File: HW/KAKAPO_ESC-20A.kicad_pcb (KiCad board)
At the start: 4 copper layers, 86.5 x 28 mm, 88 parts, among them M1 Mount_M3, M2 Mount_M3, M3 Mount_M3, M4 Mount_M3, U1 DRV8244S-Q1, U2 DRV8244S-Q1, U3 LR7533-T, U4 SK1117-ADJ, U5 STM32C011F4P6

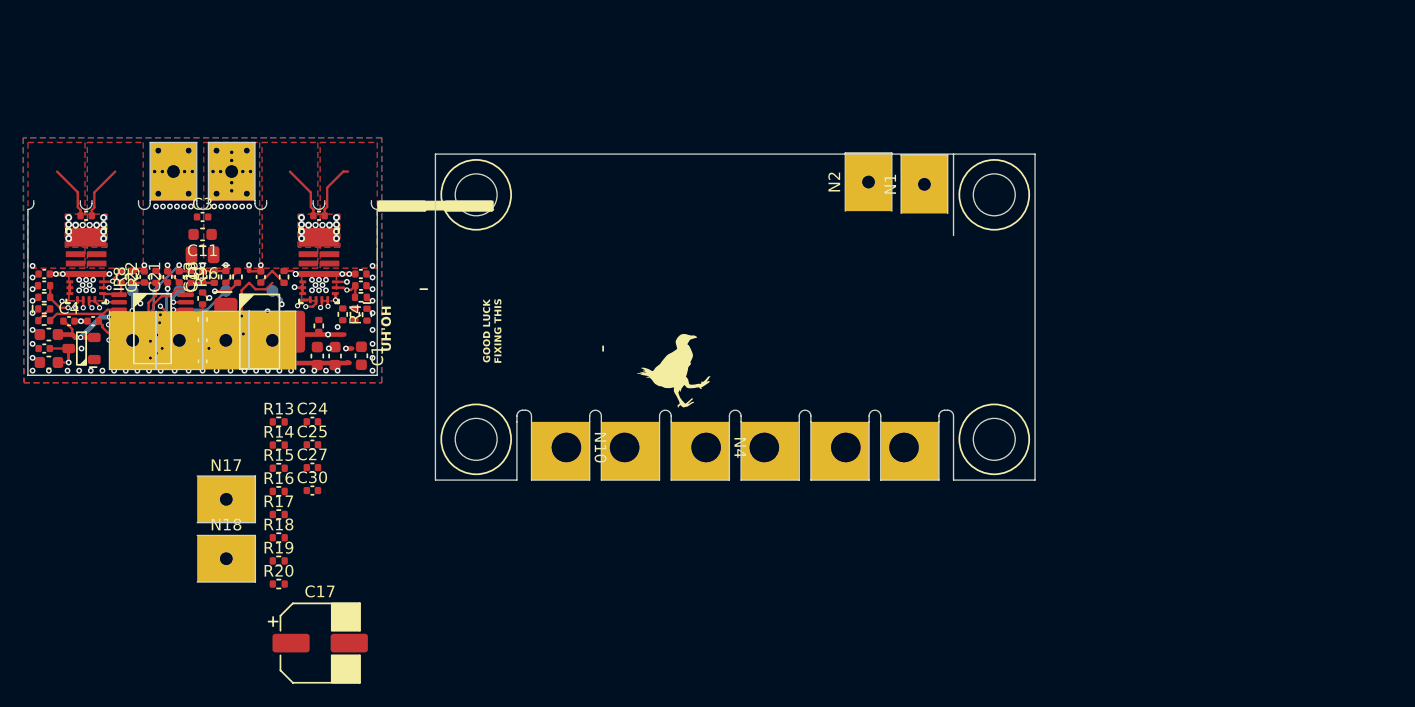
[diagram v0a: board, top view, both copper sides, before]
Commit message: WIP - Layout Motor Drivers + Buck Circuit
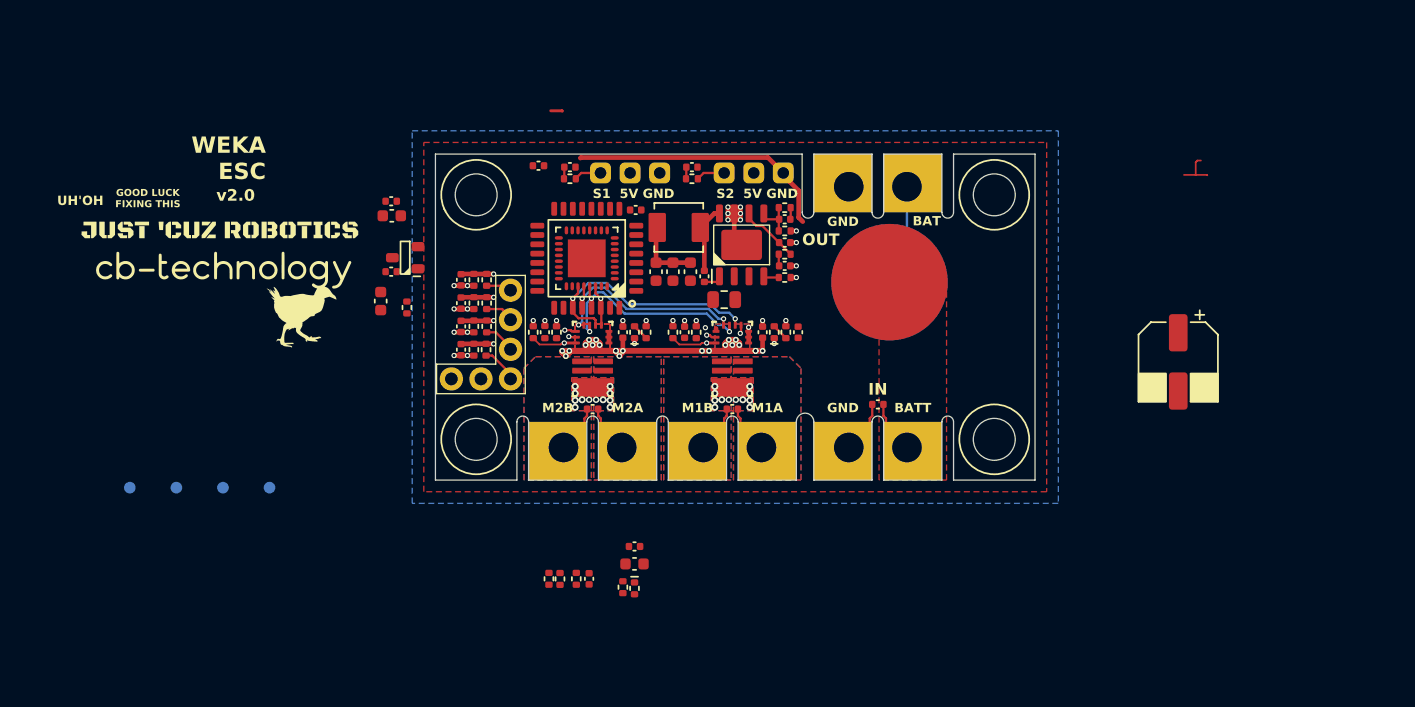
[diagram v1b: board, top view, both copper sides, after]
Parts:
- removed C10, C21: 100nF 50V, C_Capacitor:C_0402
- removed C12, C15: 22uF 10V, C_Capacitor:C_0603
- removed the G*** at (221.2, 118.8)
- removed N11, N12, N17, N18, N5, N6, N7, N8: Finger_4x5_M1, N_NonPart:Finger_4x5_M1
- removed R27: 732 1%, R_Resistor:R_0402
- removed U4: SK1117-ADJ, U_IC:SOT223_3
- added A1: Radio_FS2A, A_Assembly:Radio_FS2A, F.Cu at (200.1, 110.0)
- added C26: 100nF 50V, C_Capacitor:C_0402, F.Cu at (238.0, 121.5)
- added C31: 39pF 50V, C_Capacitor:C_0402, F.Cu at (230.0, 105.6)
- added C33: 22uF 10V, C_Capacitor:C_0603, F.Cu at (221.9, 110.1)
- added C34: 22uF 10V, C_Capacitor:C_0603, F.Cu at (220.4, 110.1)
- added C35: 22uF 10V, C_Capacitor:C_0603, F.Cu at (218.9, 110.1)
- added C37: 100nF 50V, C_Capacitor:C_0402, F.Cu at (231.2, 115.3)
- added C38: 100nF 50V, C_Capacitor:C_0402, F.Cu at (217.2, 104.8)
- added J1: Pins_2.54_1x3, J_Connector:Pins-2.54-1x3, F.Cu at (214.2, 101.6)
- added J2: Pins_2.54_1x3, J_Connector:Pins-2.54-1x3, F.Cu at (224.8, 101.6)
- added L1: 1.5uH, L_Inductor:L_4.2x4.2, F.Cu at (220.9, 106.3)
- added R21: 115.8K 1%, R_Resistor:R_0402, F.Cu at (230.0, 104.6)
- added R22: 22.1K 1%, R_Resistor:R_0402, F.Cu at (230.0, 106.6)
- added R23: 100K 1%, R_Resistor:R_0402, F.Cu at (230.0, 110.6)
- added S1: Twist_Switch_M4, CombatParts:Twist_Switch_M4, F.Cu at (239.0, 111.0)
- added U6: STM32C031KxTx, U_IC:LQFP32_08_7x7, F.Cu at (213.0, 109.0)
- added U7: STM32C031KxUx, U_IC:QFN32_05_5x5_EP, F.Cu at (213.0, 109.0)
- C1: value 22uF 10V -> 39pF 50V; footprint C_Capacitor:C_0603 -> C_Capacitor:C_0402
- C16: value 10uF 50V -> 22uF 10V; footprint C_Capacitor:C_0805 -> C_Capacitor:C_0603
- C6: value 100nF 50V -> 2.7nF 50V
- C9: value 10uF 35V -> 10uF 50V; footprint C_Capacitor:C_0603 -> C_Capacitor:C_0805
- G*** (x3), N13: moved to F.Cu
- N1, N14: moved to B.Cu
- R2: value 243 1% -> 15.8K 1%
- U5: value STM32C011F4P6 -> AP64500SP-13; footprint U_IC:TSSOP20_4.4mm -> U_IC:SOIC_8_EP
- moved C17 77.6 mm to (263.8, 117.8), turned to -90 degrees
- moved R12 51.7 mm to (218.1, 115.3), turned to -90 degrees
- moved U5 51.1 mm to (226.3, 107.8), turned to 90 degrees
- moved DS1 50.7 mm to (217.1, 115.3), turned to 90 degrees
- moved C6 50.7 mm to (230.0, 109.6), turned to 0 degrees
- moved R2 50.3 mm to (230.0, 108.6), turned to 180 degrees
- moved C20 50.0 mm to (216.1, 115.3), turned to 90 degrees
- moved R18 47.0 mm to (222.0, 102.1), turned to 180 degrees
- moved C11 46.7 mm to (217.1, 135.2)
- moved C3 46.7 mm to (217.1, 133.7)
- moved C8 46.6 mm to (213.5, 121.9), turned to 180 degrees
- moved U2 44.2 mm to (213.5, 117.6), turned to 0 degrees
- moved DS2 44.1 mm to (217.1, 137.3)
- moved R3 44.1 mm to (210.4, 115.3), turned to 90 degrees
- moved C19 43.2 mm to (209.4, 115.3), turned to 90 degrees
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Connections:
- C1 pad 1: +5V -> Net-(U5-COMP)
- C16 pad 1: VCC -> Net-(U3-VIN)
- C2 pad 1: +5V -> Net-(U3-VIN)
- C24 pad 1: VCC -> Net-(U5-BST)
- C24 pad 2: GND -> Net-(U5-SW)
- C6 pad 1: Net-(U4-VIN) -> Net-(C6-Pad1)
- C9 pad 1: Net-(U4-VIN) -> VCC
- D1 pad 1: Net-(U4-VIN) -> Net-(U3-VIN)
- D1 pad 2: VCC -> +5V
- N1 pad 1: +BATT -> Net-(C26-Pad1)
- R2 pad 1: +5V -> Net-(U5-COMP)
- R2 pad 2: Net-(U4-ADJ) -> Net-(C6-Pad1)
- U3 pad 3: +5V -> Net-(U3-VIN)
- U5 pad 1: MOTOR_B_nFAULT -> Net-(U5-BST)
- U5 pad 2: MOTOR_B_nSCS -> VCC
- U5 pad 3: LED_M2 -> VCC
- U5 pad 4: +3V3 -> Net-(U5-RT/CLK)
- U5 pad 5: GND -> Net-(U5-FB)
- U5 pad 6: /MCU/nRST -> Net-(U5-COMP)
- U5 pad 7: MOTOR_B_SNS -> GND
- U5 pad 8: RADIO_CH1 -> Net-(U5-SW)
- U5 pad 9: RADIO_CH2 -> GND
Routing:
- net +3V3: track 46.6 -> 8.24 mm, vias 6 -> 2
- net +5V: track 44.0 -> 7.03 mm, vias 3 -> 0
- net VCC: track 21.0 -> 50.6 mm, vias 31 -> 22
- net MOTOR_A_SNS: track 25.1 -> 0.92 mm, vias 2 -> 1
- net LED_M1: track 19.9 -> 0.49 mm
- net MOTOR_A_nFAULT: track 19.4 -> 0.66 mm
- net GND: track 69.6 -> 52.8 mm, vias 88 -> 51
- net (no net): track 16.5 -> 0.00 mm
- net MOTOR_A_nSCS: track 16.7 -> 0.81 mm, vias 2 -> 1
- net V_BATT: track 15.6 -> 0.00 mm, vias 2 -> 0
- net Net-(U4-VIN): track 14.2 -> 0.00 mm
- net MOTOR_B_SNS: track 14.2 -> 0.68 mm, vias 3 -> 1
- net MOTOR_SCLK: track 32.2 -> 21.4 mm, vias 3 -> 2
- net MOTOR_SDI: track 30.0 -> 19.8 mm
- net RADIO_CH2: track 12.1 -> 2.82 mm, vias 0 -> 1
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- added copper zone on In2.Cu, net GND
- added copper zone on B.Cu, net MOTOR_A+
- added copper zone on B.Cu, net MOTOR_A-
- added copper zone on B.Cu, net MOTOR_B+
- added copper zone on B.Cu, net MOTOR_B-
- added copper zone on F.Cu, net Net-(C26-Pad1)
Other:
- board size 86.5 x 28 mm -> 51.5 x 28 mm
- board text added: "BAT"
- board text added: "IN"
- board text added: "OUT"
- board text removed: "+"
- board text removed: "-"

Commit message: WIP - Continue Tracking MCU
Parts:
- added C10: 100nF 50V, C_Capacitor:C_0402, F.Cu at (238.0, 106.5)
- moved C16 11.8 mm to (206.1, 107.8), turned to 0 degrees
- moved D1 11.2 mm to (206.7, 106.6), turned to 0 degrees
- moved C5 10.6 mm to (206.1, 109.3), turned to 0 degrees
- moved C4 10.4 mm to (203.8, 111.2)
- moved C14 7.86 mm to (214.9, 96.0)
- moved C2 5.71 mm to (201.8, 111.2)
- moved U3 5.40 mm to (202.8, 109.0), turned to 90 degrees
- moved R8 2.45 mm to (203.8, 113.2), turned to 0 degrees
- moved R16 1.62 mm to (201.8, 116.2), turned to 180 degrees
- moved R9 1.55 mm to (201.8, 113.2), turned to 180 degrees
- moved R13 1.52 mm to (203.8, 114.2), turned to 180 degrees
- moved R6 1.52 mm to (203.8, 112.2), turned to 180 degrees
- moved S1 1.50 mm to (239.0, 112.5)
- moved R7 1.49 mm to (203.8, 116.2), turned to 0 degrees
- moved C13 1.46 mm to (201.8, 114.2), turned to 180 degrees
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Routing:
- net Net-(U3-VIN): track 0.00 -> 8.51 mm
- net GND: track 52.8 -> 58.5 mm, vias 51 -> 132
- net VCC: track 50.6 -> 56.2 mm
- net MOTOR_A_nFAULT: track 0.66 -> 4.57 mm
- net /MCU/PA15: track 0.00 -> 3.79 mm, vias 0 -> 1
- net Net-(U5-FB): track 7.35 -> 3.73 mm
- net MOTOR_B_nFAULT: track 1.52 -> 4.57 mm
- net LED_M2: track 0.49 -> 3.05 mm, vias 1 -> 0
- net /MCU/SWDCLK: track 0.00 -> 2.49 mm, vias 0 -> 1
- net MOTOR_B_SNS: track 0.68 -> 2.76 mm
- net MOTOR_A_SNS: track 0.92 -> 2.77 mm
- net ESC_CH1: track 2.02 -> 1.01 mm
- net +3V3: track 8.24 -> 9.06 mm, vias 2 -> 3
- net /MCU/nRST: track 0.00 -> 0.82 mm, vias 0 -> 1
- net /MCU/SWDIO: track 0.00 -> 0.82 mm, vias 0 -> 1
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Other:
- board text added: "BAT IN"
- board text removed: "BATT"
- board text removed: "IN"

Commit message: WIP - Final Detail Design Before Design Review
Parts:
- removed C11: 1uF 50V, C_Capacitor:C_0603
- removed C3: 100nF 50V, C_Capacitor:C_0402
- removed R10: 120R 1%, R_Resistor:R_0402
- added G***: LOGO, LOGO, F.Cu at (179.2, 115.8)
- added G***: LOGO, LOGO, F.Cu at (252.3, 121.7)
- added R24: 1K 1%, R_Resistor:R_1206, F.Cu at (243.6, 117.1)
- C13, C18, C22, C25: value 100nF 50V -> 1nF 50V
- DS2: footprint DS_LED:DS_0402 -> DS_LED:DS_Everlight_IR21-21CL110TR8
- moved TP2 47.9 mm to (217.5, 109.2)
- moved TP4 39.8 mm to (212.5, 109.2)
- moved DS2 37.7 mm to (245.5, 112.5)
- moved TP1 35.1 mm to (215.0, 109.2)
- moved TP3 34.3 mm to (210.0, 109.2)
- moved D2 26.0 mm to (221.1, 112.1), turned to 0 degrees
- moved C23 25.1 mm to (219.1, 112.1), turned to 180 degrees
- moved R19 23.7 mm to (208.7, 112.8), turned to 0 degrees
- moved R20 22.8 mm to (208.7, 113.8), turned to 180 degrees
- moved C17 10.5 mm to (257.5, 109.4), turned to 90 degrees
- moved C14 9.18 mm to (217.2, 104.9)
- moved C9 5.86 mm to (230.0, 109.8), turned to 90 degrees
- moved C38 4.90 mm to (221.0, 101.7), turned to 90 degrees
- moved C6 3.26 mm to (231.5, 106.7), turned to 90 degrees
- moved R23 1.50 mm to (231.5, 110.5), turned to -90 degrees
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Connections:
- S1 pad 1: Net-(C26-Pad1) -> VCC
- S1 pad 2: VCC -> Net-(C26-Pad1)
- U6 pad 1: /MCU/PB9 -> MOTOR_A_nSCS
- U6 pad 19: /MCU/PA9 -> RADIO_CH1
- U6 pad 2: /MCU/PC14 -> LED_M1
- U6 pad 20: /MCU/PC6 -> RADIO_CH2
- U6 pad 21: /MCU/PA10 -> RADIO_CH3
- U6 pad 22: /MCU/PA11 -> RADIO_CH4
- U6 pad 23: /MCU/PA12 -> V_BATT
- U6 pad 26: /MCU/PA15 -> MOTOR_B_nFAULT
- U6 pad 31: /MCU/PB7 -> LED_M2
- U6 pad 32: /MCU/PB8 -> MOTOR_A_nFAULT
- U7 pad 1: /MCU/PB9 -> MOTOR_A_nSCS
- U7 pad 19: /MCU/PA9 -> RADIO_CH1
- U7 pad 2: /MCU/PC14 -> LED_M1
- U7 pad 20: /MCU/PC6 -> RADIO_CH2
- U7 pad 21: /MCU/PA10 -> RADIO_CH3
- U7 pad 22: /MCU/PA11 -> RADIO_CH4
- U7 pad 23: /MCU/PA12 -> V_BATT
- U7 pad 26: /MCU/PA15 -> MOTOR_B_nFAULT
- U7 pad 31: /MCU/PB7 -> LED_M2
- U7 pad 32: /MCU/PB8 -> MOTOR_A_nFAULT
- U7 pad 33: unconnected-(U7-EP-Pad33) -> GND
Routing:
- net GND: track 58.5 -> 177.1 mm, vias 132 -> 163
- net VCC: track 56.2 -> 103.7 mm, vias 22 -> 30
- net +3V3: track 9.06 -> 40.9 mm, vias 3 -> 4
- net LED_M1: track 0.49 -> 18.1 mm, vias 1 -> 2
- net +5V: track 7.65 -> 24.8 mm
- net Net-(C23-Pad1): track 0.00 -> 14.3 mm, vias 0 -> 2
- net MOTOR_A_nSCS: track 0.81 -> 15.1 mm, vias 1 -> 2
- net RADIO_CH4: track 2.02 -> 15.4 mm, vias 1 -> 2
- net RADIO_CH3: track 2.01 -> 13.9 mm, vias 1 -> 2
- net RADIO_CH2: track 2.02 -> 13.6 mm, vias 1 -> 2
- net RADIO_CH1: track 2.01 -> 12.4 mm, vias 1 -> 2
- net MOTOR_A_nFAULT: track 4.57 -> 12.3 mm, vias 2 -> 3
- net /MCU/nRST: track 0.82 -> 7.52 mm, vias 1 -> 2
- net V_BATT: track 0.00 -> 5.97 mm
- net MOTOR_B_nFAULT: track 4.57 -> 10.3 mm
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- added copper zone on F.Cu, net +5V
- added copper zone on B.Cu, net Net-(C26-Pad1)
- removed copper zone on F.Cu, net Net-(C26-Pad1)
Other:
- outline, holes or cut-outs redrawn
- board text removed: "GOOD LUCK FIXING THIS"
- board text removed: "UH'OH"

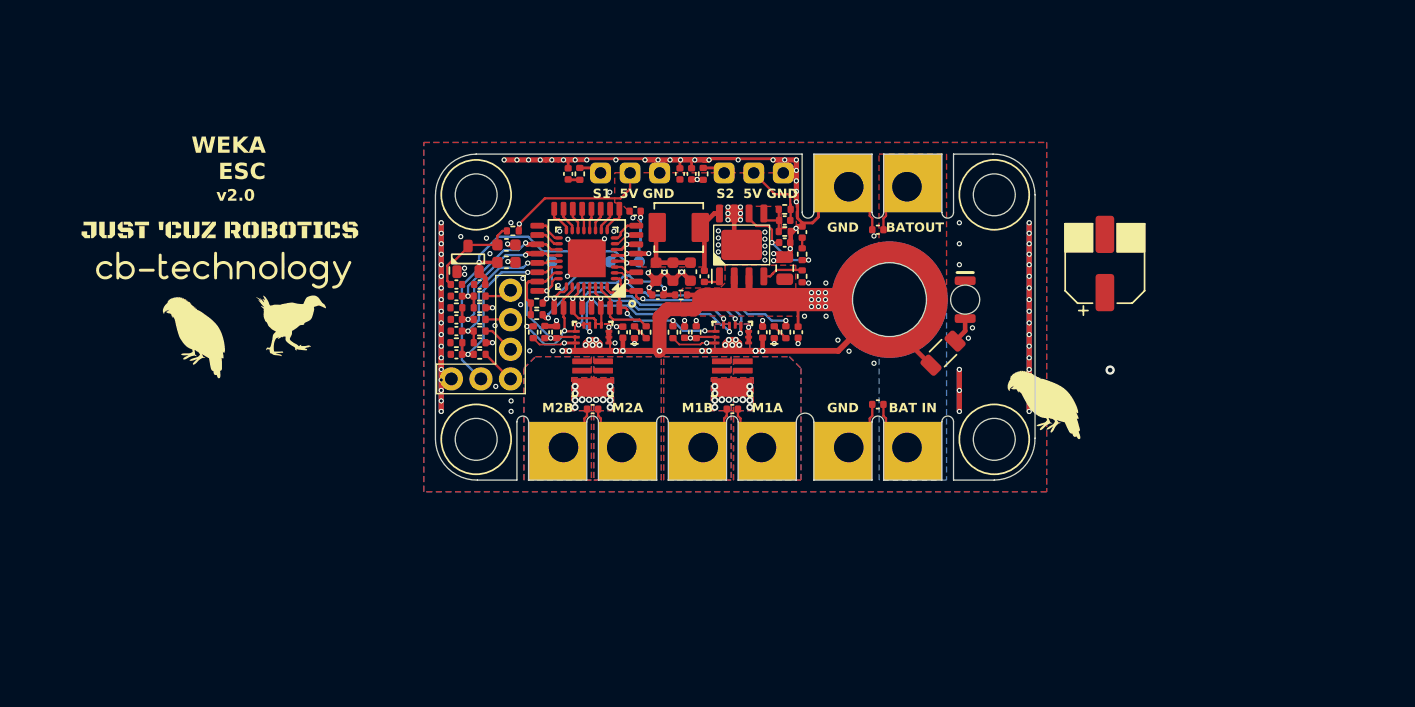
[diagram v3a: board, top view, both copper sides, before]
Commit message: Move 5V Supply Around To Make More Efficient Conduction Path
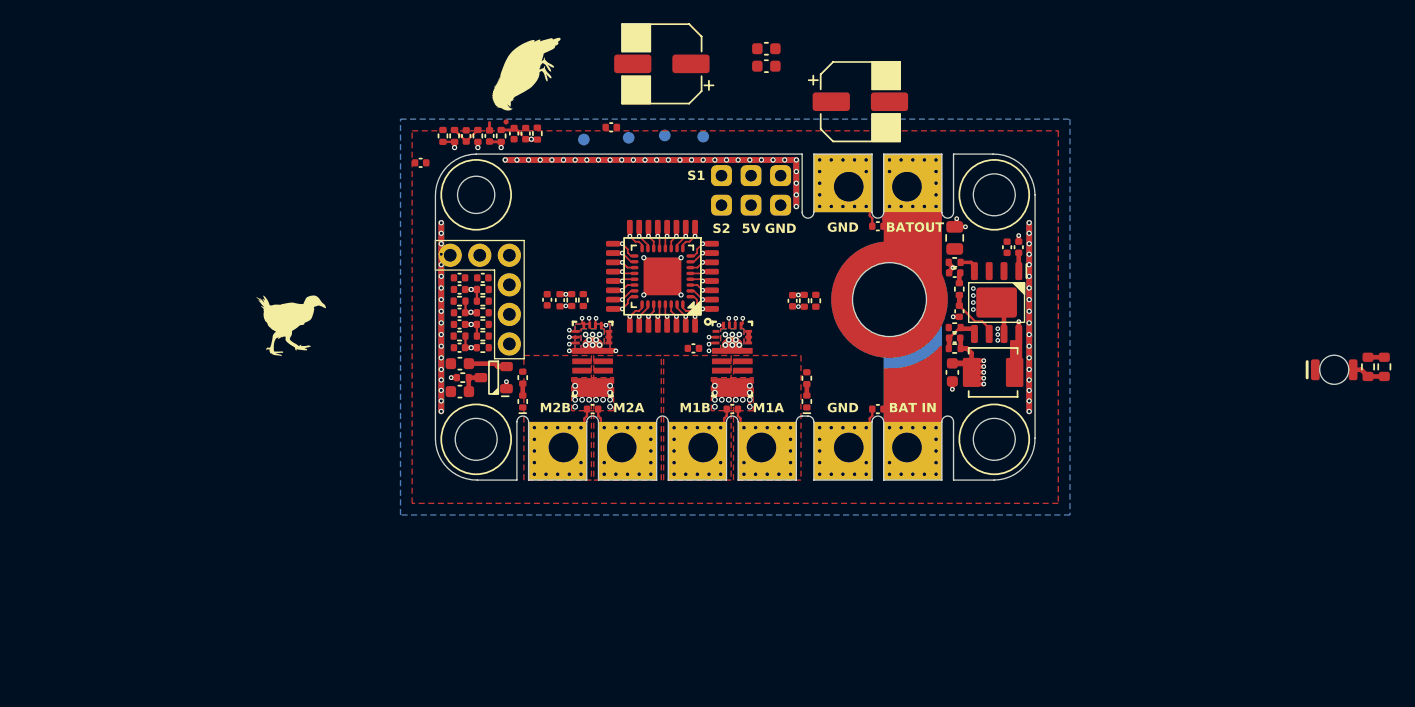
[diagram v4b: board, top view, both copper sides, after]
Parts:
- removed C17: 220uF 50V, C_Capacitor:C_6.3mm_SMD
- added C11: 220uF, 35V, C_Capacitor:C_6.3mm_SMD, F.Cu at (236.5, 95.5)
- added C12: 220uF, 35V, C_Capacitor:C_6.3mm_SMD, F.Cu at (219.4, 92.2)
- added C3: 100nF 50V, C_Capacitor:C_0402, F.Cu at (198.7, 100.8)
- added R10: 2.2K 5%, R_Resistor:R_0603, F.Cu at (281.5, 118.3)
- C27, C30: value 100nF 50V -> 1nF 50V
- G*** (x3): moved to B.Cu
- R24: value 1K 1% -> 2.2K 5%; footprint R_Resistor:R_1206 -> R_Resistor:R_0603
- moved G*** 52.8 mm to (207.9, 93.1), turned to 105 degrees
- moved G*** 49.8 mm to (228.8, 111.4), turned to 180 degrees
- moved G*** 41.4 mm to (221.0, 119.5), turned to 180 degrees
- moved G*** 38.8 mm to (220.0, 117.0), turned to 180 degrees
- moved R24 36.5 mm to (280.1, 118.3), turned to -90 degrees
- moved DS2 32.3 mm to (277.2, 118.5), turned to 0 degrees
- moved L1 29.7 mm to (247.9, 118.8)
- moved C24 27.1 mm to (250.1, 108.0)
- moved C33 24.1 mm to (244.4, 118.8)
- moved U5 22.5 mm to (248.2, 112.8), turned to -90 degrees
- moved D2 22.2 mm to (203.6, 98.4), turned to -90 degrees
- moved C23 21.4 mm to (202.6, 98.4), turned to 90 degrees
- moved C35 21.4 mm to (228.4, 91.0), turned to 180 degrees
- moved C34 19.4 mm to (228.4, 92.5), turned to 180 degrees
- moved C37 19.4 mm to (249.1, 108.0), turned to 90 degrees
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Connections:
- U6 pad 1: MOTOR_A_nSCS -> /MCU/PB9
- U6 pad 11: /MCU/PA4 -> ESC_CH2
- U6 pad 12: /MCU/PA5 -> ESC_CH1
- U6 pad 16: /MCU/PB1 -> V_BATT
- U6 pad 18: /MCU/PA8 -> RADIO_CH1
- U6 pad 19: RADIO_CH1 -> RADIO_CH2
- U6 pad 20: RADIO_CH2 -> RADIO_CH3
- U6 pad 21: RADIO_CH3 -> RADIO_CH4
- U6 pad 22: RADIO_CH4 -> MOTOR_B_SNS
- U6 pad 23: V_BATT -> LED_M2
- U6 pad 30: MOTOR_B_nSCS -> MOTOR_A_SNS
- U6 pad 31: LED_M2 -> MOTOR_A_nSCS
- U7 pad 1: MOTOR_A_nSCS -> /MCU/PB9
- U7 pad 11: /MCU/PA4 -> ESC_CH2
- U7 pad 12: /MCU/PA5 -> ESC_CH1
- U7 pad 16: /MCU/PB1 -> V_BATT
- U7 pad 18: /MCU/PA8 -> RADIO_CH1
- U7 pad 19: RADIO_CH1 -> RADIO_CH2
- U7 pad 20: RADIO_CH2 -> RADIO_CH3
- U7 pad 21: RADIO_CH3 -> RADIO_CH4
- U7 pad 22: RADIO_CH4 -> MOTOR_B_SNS
- U7 pad 23: V_BATT -> LED_M2
- U7 pad 30: MOTOR_B_nSCS -> MOTOR_A_SNS
- U7 pad 31: LED_M2 -> MOTOR_A_nSCS
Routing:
- net GND: track 177.1 -> 269.3 mm, vias 163 -> 138
- net VCC: track 103.7 -> 25.7 mm, vias 30 -> 34
- net +3V3: track 40.9 -> 7.03 mm, vias 4 -> 3
- net MOTOR_SCLK: track 21.1 -> 3.14 mm, vias 2 -> 3
- net MOTOR_SDI: track 19.4 -> 3.15 mm
- net LED_M1: track 18.1 -> 2.58 mm, vias 2 -> 1
- net MOTOR_SDO: track 19.0 -> 3.51 mm
- net MOTOR_A_nSCS: track 15.1 -> 2.91 mm
- net +5V: track 24.8 -> 13.1 mm, vias 1 -> 6
- net Net-(C23-Pad1): track 14.3 -> 2.82 mm, vias 2 -> 0
- net RADIO_CH4: track 15.4 -> 3.95 mm
- net RADIO_CH3: track 13.9 -> 3.92 mm
- net MOTOR_A_nFAULT: track 12.3 -> 2.46 mm, vias 3 -> 1
- net RADIO_CH2: track 13.6 -> 4.06 mm
- net RADIO_CH1: track 12.4 -> 4.17 mm
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- removed copper zone on F.Cu, net +5V
- removed copper zone on B.Cu, net GND
- removed copper zone on B.Cu, net MOTOR_A+
- removed copper zone on B.Cu, net MOTOR_A-
- removed copper zone on B.Cu, net MOTOR_B+
- removed copper zone on B.Cu, net MOTOR_B-
- removed copper zone on B.Cu, net Net-(C26-Pad1)
- removed copper zone on In1.Cu, net VCC
- removed copper zone on In2.Cu, net VCC
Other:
- outline, holes or cut-outs redrawn
- board text added: "BAT OUT"
- board text added: "KAKAPO ESC v1.0"
- board text removed: "WEKA ESC"
- board text removed: "v2.0"
